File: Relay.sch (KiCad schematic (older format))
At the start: 11 parts

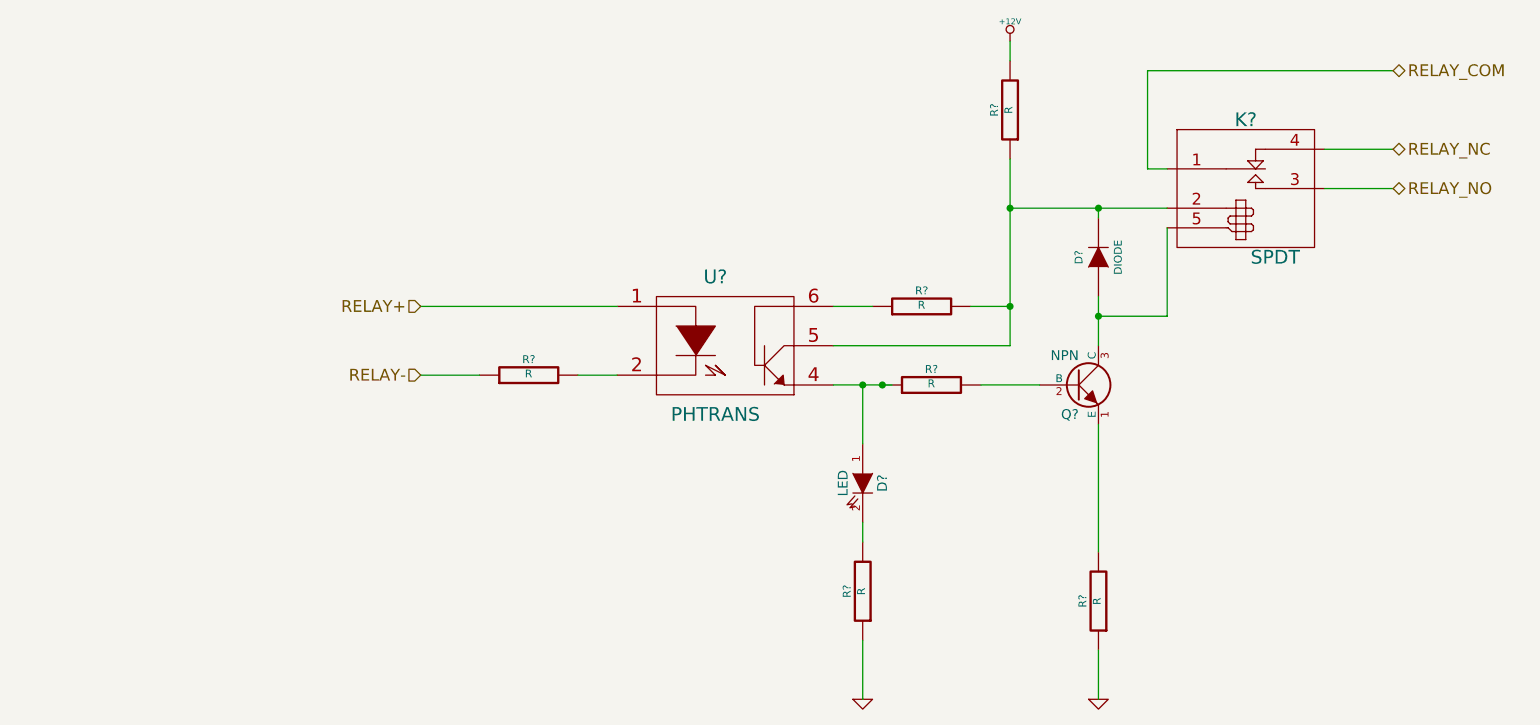
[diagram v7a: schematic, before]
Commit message: RELAY 02-20-2014
1) Created and associated footprints for relay module
2) Placed relay module's components in PCB layout
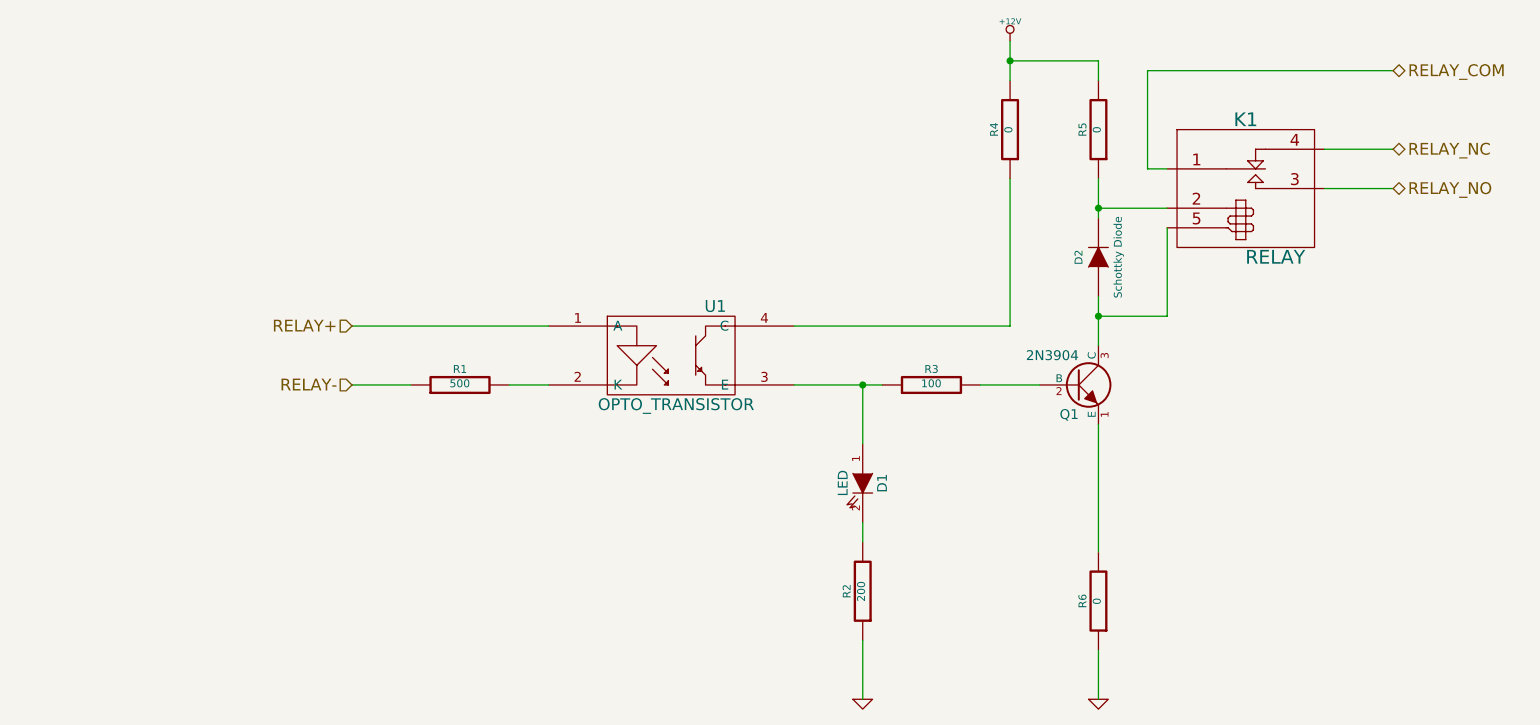
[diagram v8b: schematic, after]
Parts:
- removed R?: R, ~, symbol R
- removed U?: PHTRANS, ~, symbol PHTRANS
- added R5: 0, ~, symbol R
- added U1: OPTO_TRANSISTOR, symbol OPTO-TRANSISTOR4
- D1: renamed from D?; MFG NAME (none) -> OSRAM; MFG PART NUM (none) -> LG Q971-KN-1
- D2: renamed from D?; value DIODE -> Schottky Diode; MFG NAME (none) -> Diodes Inc; MFG PART NUM (none) -> B130-13-F
- K1: renamed from K?; value SPDT -> RELAY; MFG NAME (none) -> TE Connectivity; MFG PART NUM (none) -> 1461069-5
- Q1: renamed from Q?; value NPN -> 2N3904; MFG NAME (none) -> Diodes Inc; MFG PART NUM (none) -> MMBT3904-7-F
- R1: renamed from R?; value R -> 500
- R2: renamed from R?; value R -> 200
- R3: renamed from R?; value R -> 100
- R4, R6: renamed from R?; value R -> 0
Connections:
- wire segments 25 -> 26
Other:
- moved on the sheet: R1, R4
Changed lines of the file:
@@
 Sheet 7 9
 Title ""
-Date "11 feb 2014"
+Date "20 feb 2014"
 Rev ""
 Comp ""
@@
 Comment4 ""
 $EndDescr
-Text HLabel 4400 3400 0    60   Input ~ 0
+Text HLabel 4050 3500 0    60   Input ~ 0
 RELAY+
-Text HLabel 4400 3750 0    60   Input ~ 0
+Text HLabel 4050 3800 0    60   Input ~ 0
 RELAY-
 Text HLabel 9350 2600 2    60   BiDi ~ 0
@@
 RELAY_NO
 $Comp
-L PHTRANS U?
-U 1 1 52F74091
-P 5950 3600
-F 0 "U?" H 5900 3950 70  0000 C CNN
-F 1 "PHTRANS" H 5900 3250 70  0000 C CNN
-F 2 "~" H 5950 3600 60  0000 C CNN
-F 3 "~" H 5950 3600 60  0000 C CNN
-	1    5950 3600
-	1    0    0    -1
-$EndComp
-$Comp
-L R R?
+L R R3
 U 1 1 52F740A0
 P 7000 3800
-F 0 "R?" V 7080 3800 40  0000 C CNN
-F 1 "R" V 7007 3801 40  0000 C CNN
+F 0 "R3" V 7080 3800 40  0000 C CNN
+F 1 "100" V 7007 3801 40  0000 C CNN
 F 2 "~" V 6930 3800 30  0000 C CNN
 F 3 "~" H 7000 3800 30  0000 C CNN
@@
 $EndComp
 $Comp
-L NPN Q?
+L NPN Q1
 U 1 1 52F740AF
 P 7750 3800
-F 0 "Q?" H 7750 3650 50  0000 R CNN
-F 1 "NPN" H 7750 3950 50  0000 R CNN
+F 0 "Q1" H 7750 3650 50  0000 R CNN
+F 1 "2N3904" H 7750 3950 50  0000 R CNN
 F 2 "~" H 7750 3800 60  0000 C CNN
 F 3 "~" H 7750 3800 60  0000 C CNN
+F 4 "Diodes Inc" H 7750 3800 60  0001 C CNN "MFG NAME"
+F 5 "MMBT3904-7-F" H 7750 3800 60  0001 C CNN "MFG PART NUM"
 	1    7750 3800
 	1    0    0    -1
 $EndComp
 $Comp
-L LED D?
+L LED D1
 U 1 1 52F740BE
 P 6650 4300
-F 0 "D?" H 6650 4400 50  0000 C CNN
+F 0 "D1" H 6650 4400 50  0000 C CNN
 F 1 "LED" H 6650 4200 50  0000 C CNN
 F 2 "~" H 6650 4300 60  0000 C CNN
 F 3 "~" H 6650 4300 60  0000 C CNN
+F 4 "OSRAM" H 6650 4300 60  0001 C CNN "MFG NAME"
+F 5 "LG Q971-KN-1" H 6650 4300 60  0001 C CNN "MFG PART NUM"
 	1    6650 4300
 	0    1    1    0
 $EndComp
 $Comp
-L SPDT K?
+L SPDT K1
 U 1 1 52F7444C
 P 8600 2650
-F 0 "K?" H 8600 2850 70  0000 C CNN
-F 1 "SPDT" H 8750 2150 70  0000 C CNN
+F 0 "K1" H 8600 2850 70  0000 C CNN
+F 1 "RELAY" H 8750 2150 70  0000 C CNN
 F 2 "~" H 8600 2650 60  0000 C CNN
 F 3 "~" H 8600 2650 60  0000 C CNN
+F 4 "TE Connectivity" H 8600 2650 60  0001 C CNN "MFG NAME"
+F 5 "1461069-5" H 8600 2650 60  0001 C CNN "MFG PART NUM"
 	1    8600 2650
 	1    0    0    -1
@@
 	8100 2700 8200 2700
 Wire Wire Line
-	6500 3800 6800 3800
-Connection ~ 6750 3800
+	6300 3800 6750 3800
 Wire Wire Line
 	7250 3800 7550 3800
@@
 	7850 4000 7850 4650
 $Comp
-L R R?
+L R R6
 U 1 1 52F744D2
 P 7850 4900
-F 0 "R?" V 7930 4900 40  0000 C CNN
-F 1 "R" V 7857 4901 40  0000 C CNN
+F 0 "R6" V 7930 4900 40  0000 C CNN
+F 1 "0" V 7857 4901 40  0000 C CNN
 F 2 "~" V 7780 4900 30  0000 C CNN
 F 3 "~" H 7850 4900 30  0000 C CNN
@@
 $EndComp
 $Comp
-L GND #PWR?
+L GND #PWR44
 U 1 1 52F744DA
 P 7850 5400
-F 0 "#PWR?" H 7850 5400 30  0001 C CNN
+F 0 "#PWR44" H 7850 5400 30  0001 C CNN
 F 1 "GND" H 7850 5330 30  0001 C CNN
 F 2 "" H 7850 5400 60  0000 C CNN
@@
 	7850 5400 7850 5150
 $Comp
-L R R?
+L R R2
 U 1 1 52F744FD
 P 6650 4850
-F 0 "R?" V 6730 4850 40  0000 C CNN
-F 1 "R" V 6657 4851 40  0000 C CNN
+F 0 "R2" V 6730 4850 40  0000 C CNN
+F 1 "200" V 6657 4851 40  0000 C CNN
 F 2 "~" V 6580 4850 30  0000 C CNN
 F 3 "~" H 6650 4850 30  0000 C CNN
@@
 	6650 4500 6650 4600
 $Comp
-L GND #PWR?
+L GND #PWR42
 U 1 1 52F7451F
 P 6650 5400
-F 0 "#PWR?" H 6650 5400 30  0001 C CNN
+F 0 "#PWR42" H 6650 5400 30  0001 C CNN
 F 1 "GND" H 6650 5330 30  0001 C CNN
 F 2 "" H 6650 5400 60  0000 C CNN
@@
 	6650 5400 6650 5100
 $Comp
-L +12V #PWR?
+L +12V #PWR43
 U 1 1 52F74537
 P 7400 2050
-F 0 "#PWR?" H 7400 2000 20  0001 C CNN
+F 0 "#PWR43" H 7400 2000 20  0001 C CNN
 F 1 "+12V" H 7400 2150 30  0000 C CNN
 F 2 "" H 7400 2050 60  0000 C CNN
@@
 $EndComp
 $Comp
-L R R?
+L R R4
 U 1 1 52F74544
-P 7400 2400
-F 0 "R?" V 7480 2400 40  0000 C CNN
-F 1 "R" V 7407 2401 40  0000 C CNN
-F 2 "~" V 7330 2400 30  0000 C CNN
-F 3 "~" H 7400 2400 30  0000 C CNN
-	1    7400 2400
-	-1   0    0    1
-$EndComp
-Wire Wire Line
-	7400 2050 7400 2150
-Wire Wire Line
-	7400 2650 7400 3600
-Wire Wire Line
-	7400 2900 8200 2900
-Wire Wire Line
-	7400 3600 6500 3600
-Connection ~ 7400 2900
-$Comp
-L R R?
-U 1 1 52F74581
-P 6950 3400
-F 0 "R?" V 7030 3400 40  0000 C CNN
-F 1 "R" V 6957 3401 40  0000 C CNN
-F 2 "~" V 6880 3400 30  0000 C CNN
-F 3 "~" H 6950 3400 30  0000 C CNN
-	1    6950 3400
+P 7400 2500
+F 0 "R4" V 7480 2500 40  0000 C CNN
+F 1 "0" V 7407 2501 40  0000 C CNN
+F 2 "~" V 7330 2500 30  0000 C CNN
+F 3 "~" H 7400 2500 30  0000 C CNN
+	1    7400 2500
+	-1   0    0    1
+$EndComp
+Wire Wire Line
+	7400 2050 7400 2250
+Wire Wire Line
+	7400 3500 7400 2750
+Wire Wire Line
+	7850 2900 8200 2900
+Wire Wire Line
+	6300 3500 7400 3500
+$Comp
+L R R1
+U 1 1 52F745B4
+P 4600 3800
+F 0 "R1" V 4680 3800 40  0000 C CNN
+F 1 "500" V 4607 3801 40  0000 C CNN
+F 2 "~" V 4530 3800 30  0000 C CNN
+F 3 "~" H 4600 3800 30  0000 C CNN
+	1    4600 3800
 	0    -1   -1   0
 $EndComp
 Wire Wire Line
-	6700 3400 6500 3400
-Wire Wire Line
-	7200 3400 7400 3400
-Connection ~ 7400 3400
-$Comp
-L R R?
-U 1 1 52F745B4
-P 4950 3750
-F 0 "R?" V 5030 3750 40  0000 C CNN
-F 1 "R" V 4957 3751 40  0000 C CNN
-F 2 "~" V 4880 3750 30  0000 C CNN
-F 3 "~" H 4950 3750 30  0000 C CNN
-	1    4950 3750
-	0    -1   -1   0
-$EndComp
-Wire Wire Line
-	5400 3750 5200 3750
-Wire Wire Line
-	5400 3400 4400 3400
-Wire Wire Line
-	4700 3750 4400 3750
+	5050 3800 4850 3800
+Wire Wire Line
+	5050 3500 4050 3500
+Wire Wire Line
+	4350 3800 4050 3800
 Wire Wire Line
 	8200 3450 8200 3000
 $Comp
-L DIODE D?
+L DIODE D2
 U 1 1 52F7462E
 P 7850 3150
-F 0 "D?" H 7850 3250 40  0000 C CNN
-F 1 "DIODE" H 7850 3050 40  0000 C CNN
+F 0 "D2" H 7850 3250 40  0000 C CNN
+F 1 "Schottky Diode" H 7850 3050 40  0000 C CNN
 F 2 "~" H 7850 3150 60  0000 C CNN
 F 3 "~" H 7850 3150 60  0000 C CNN
+F 4 "Diodes Inc" H 7850 3150 60  0001 C CNN "MFG NAME"
+F 5 "B130-13-F" H 7850 3150 60  0001 C CNN "MFG PART NUM"
 	1    7850 3150
 	0    -1   -1   0
 $EndComp
 Wire Wire Line
-	7850 2950 7850 2900
+	7850 2750 7850 2950
 Connection ~ 7850 2900
 Connection ~ 7850 3450
+$Comp
+L OPTO-TRANSISTOR4 U1
+U 1 1 5305B074
+P 5700 3650
+F 0 "U1" H 5900 3900 60  0000 C CNN
+F 1 "OPTO_TRANSISTOR" H 5700 3400 60  0000 C CNN
+F 2 "" H 5700 3650 60  0000 C CNN
+F 3 "" H 5700 3650 60  0000 C CNN
+F 4 "LITE-ON" H 5700 3650 60  0001 C CNN "MFG NAME"
+F 5 "LTV-816S" H 5700 3650 60  0001 C CNN "MFG PART NUM"
+	1    5700 3650
+	1    0    0    -1
+$EndComp
+Wire Wire Line
+	6500 3500 6500 3500
+$Comp
+L R R5
+U 1 1 5305B277
+P 7850 2500
+F 0 "R5" V 7930 2500 40  0000 C CNN
+F 1 "0" V 7857 2501 40  0000 C CNN
+F 2 "~" V 7780 2500 30  0000 C CNN
+F 3 "~" H 7850 2500 30  0000 C CNN
+	1    7850 2500
+	-1   0    0    1
+$EndComp
+Wire Wire Line
+	7850 2250 7850 2150
+Wire Wire Line
+	7850 2150 7400 2150
+Connection ~ 7400 2150
 $EndSCHEMATC
